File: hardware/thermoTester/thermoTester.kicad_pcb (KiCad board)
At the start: 2 copper layers, 100 x 100 mm, 157 parts, among them J10 Power, J20 PRG, J21 relay, J22 relay, J40 temperature, J41 grating, J42 load, J43 PM9808_TR, J44 key_in, J45 key_in, J46 lamp, J47 lamp, J48 CPTTL, J50 bough, Q30 BC817, Q31 BC817, Q32 BC817, Q50 BC817, Q51 BC817, Q52 BC817, Q53 BC807, Q54 BC817, Q55 BC817, Q56 AO3400, Q60 BC817, Q61 BC817, Q62 BC817, Q63 BC817, Q64 BC817, Q65 BC817, Q66 BC817, U10 XL1509, U11 LM1117-3.3, U20 M_STM32F103RCT6, U21 ULN2003, U22 ULN2003, U40 SP3232, U41 SP3485CN, U50 EL3H4B, Y20 12M

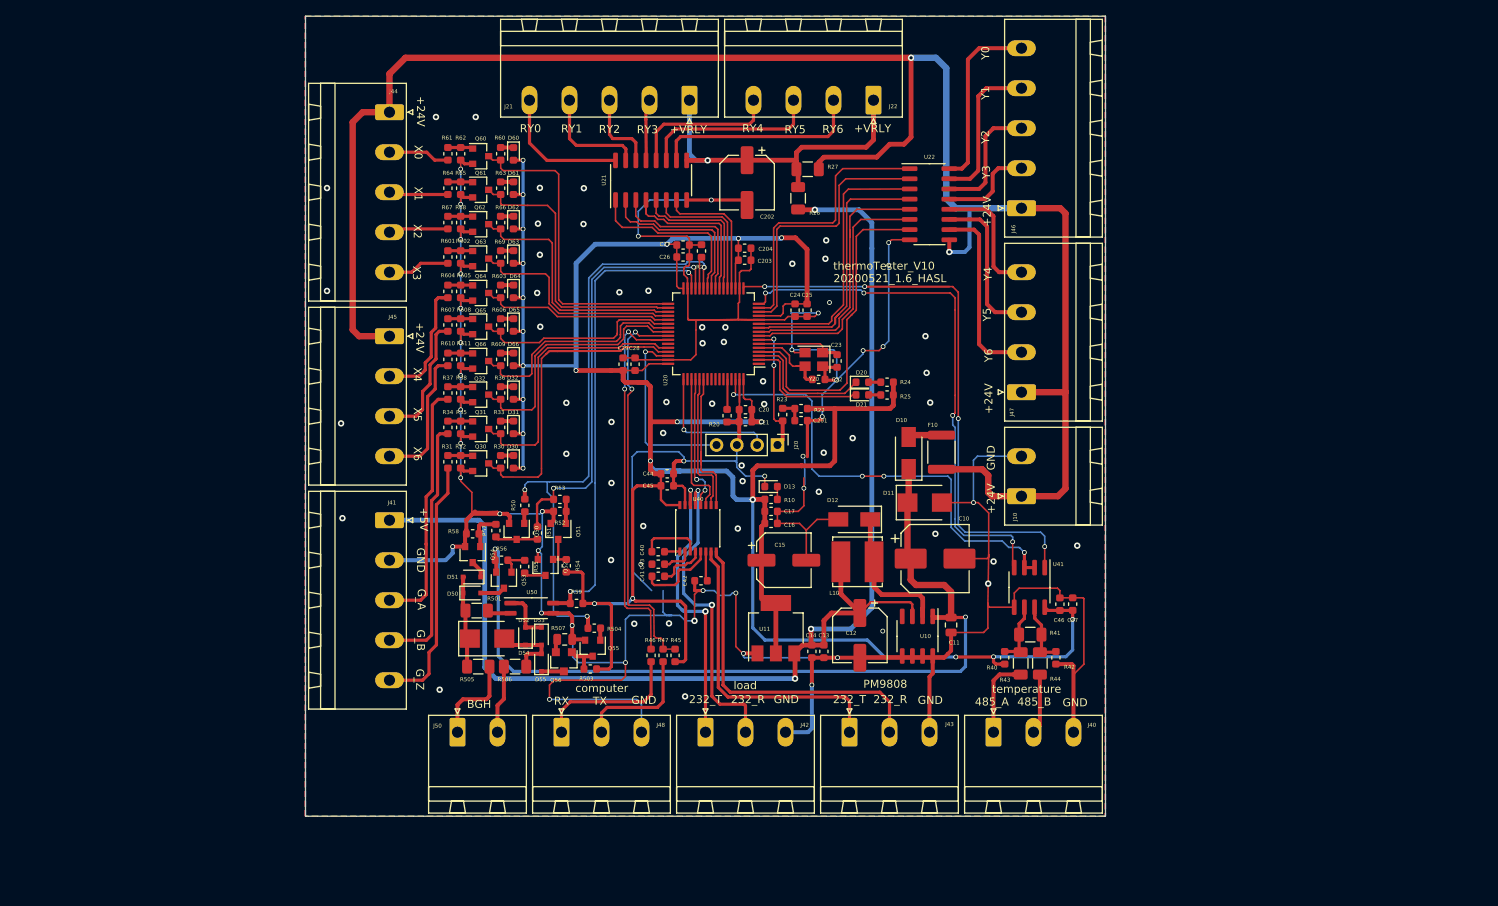
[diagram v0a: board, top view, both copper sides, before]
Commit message: 修改pcb文件，增加外壳支持
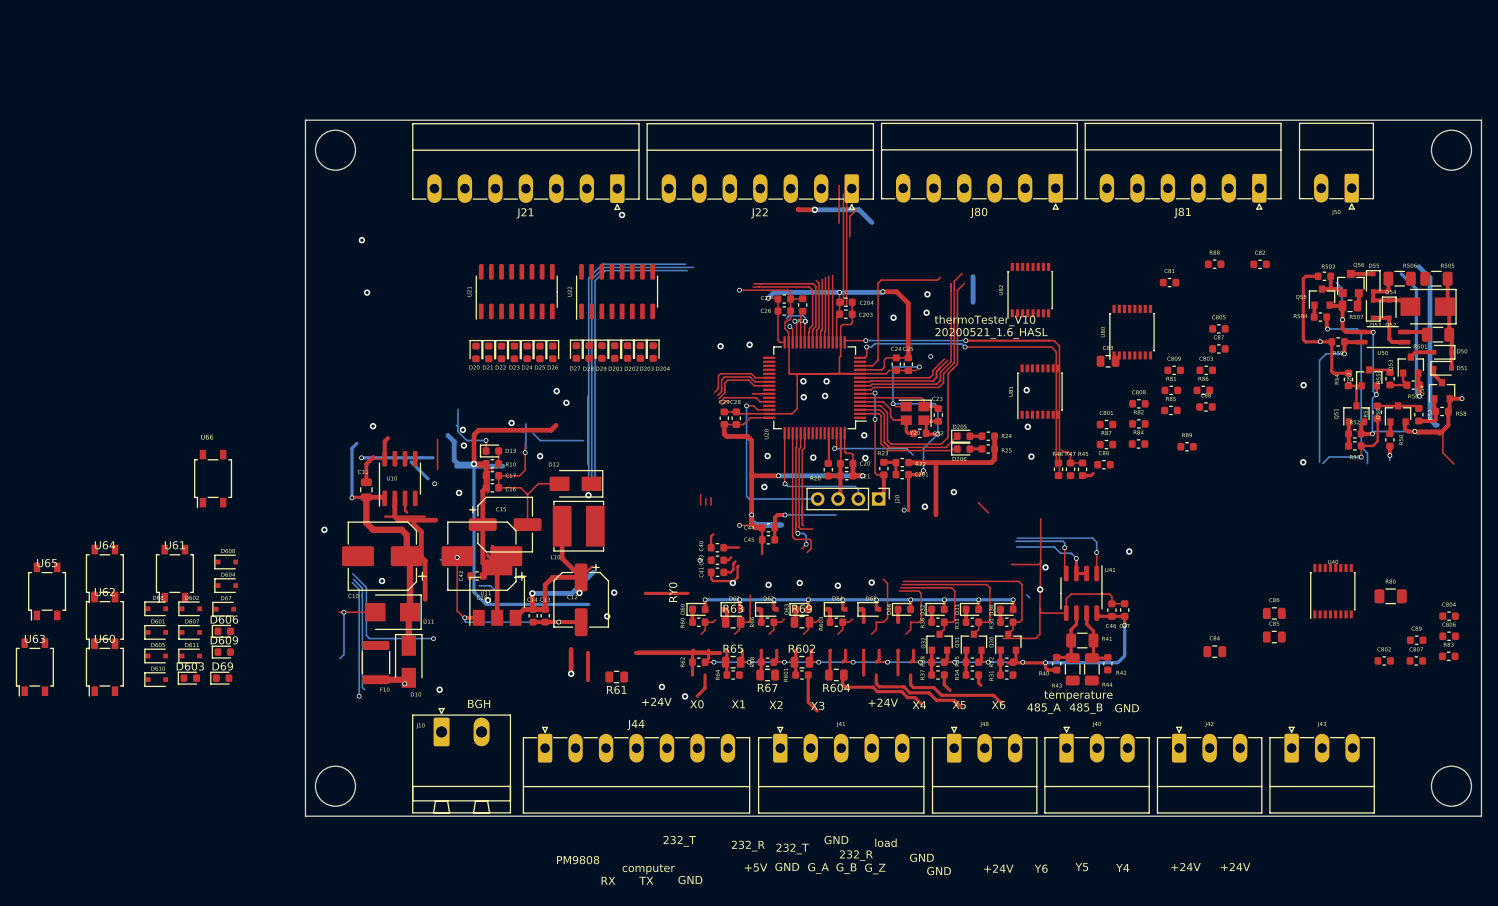
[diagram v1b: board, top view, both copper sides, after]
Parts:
- removed C202: 220uF, kicad_footprint_general:CP_Elec_6.3x5.4
- removed J45: key_in, kicad_footprint_general:PhoenixContact_MSTBA_2,5_4-G_1x04_P5.00mm_Horizontal
- removed J46: lamp, kicad_footprint_general:PhoenixContact_MSTBA_2,5_5-G_1x05_P5.00mm_Horizontal
- removed J47: lamp, kicad_footprint_general:PhoenixContact_MSTBA_2,5_4-G_1x04_P5.00mm_Horizontal
- removed Q60, Q61, Q62, Q63, Q64, Q65, Q66: BC817, kicad_footprint_general:SOT-23
- removed R26: 0, kicad_footprint_general:R_1206_3216Metric
- removed R27: NP(0), kicad_footprint_general:R_1206_3216Metric
- removed R605, R606, R607, R608, R609, R610, R611: 10k, kicad_footprint_general:R_0603_1608Metric
- added C18: 47uF, kicad_footprint_general:CP_Elec_8x6.5, F.Cu at (72.0, 117.5)
- added C80: 47nF, kicad_footprint_general:C_0603_1608Metric, F.Cu at (149.8, 106.1)
- added C801: 47nF, kicad_footprint_general:C_0603_1608Metric, F.Cu at (150.1, 101.0)
- added C802: 47nF, kicad_footprint_general:C_0603_1608Metric, F.Cu at (184.8, 130.6)
- added C803: 47nF, kicad_footprint_general:C_0603_1608Metric, F.Cu at (162.6, 94.3)
- added C804: 47nF, kicad_footprint_general:C_0603_1608Metric, F.Cu at (192.9, 125.0)
- added C805: 47nF, kicad_footprint_general:C_0603_1608Metric, F.Cu at (164.2, 89.1)
- added C806: 100nF, kicad_footprint_general:C_0603_1608Metric, F.Cu at (192.9, 127.5)
- added C807: 1uF, kicad_footprint_general:C_0603_1608Metric, F.Cu at (188.9, 130.6)
- added C808: 1uF, kicad_footprint_general:C_0603_1608Metric, F.Cu at (154.2, 98.5)
- added C809: 100nF, kicad_footprint_general:C_0603_1608Metric, F.Cu at (158.6, 94.3)
- added C81: 47nF, kicad_footprint_general:C_0603_1608Metric, F.Cu at (158.0, 83.3)
- added C82: 47nF, kicad_footprint_general:C_0603_1608Metric, F.Cu at (169.3, 81.0)
- added C83: 100nF, kicad_footprint_general:C_0805_2012Metric, F.Cu at (150.3, 93.1)
- added C84: 100nF, kicad_footprint_general:C_0805_2012Metric, F.Cu at (163.7, 129.4)
- added C85: 100nF, kicad_footprint_general:C_0805_2012Metric, F.Cu at (171.1, 127.6)
- added C86: 100nF, kicad_footprint_general:C_0805_2012Metric, F.Cu at (171.1, 124.7)
- added C87: 47nF, kicad_footprint_general:C_0603_1608Metric, F.Cu at (164.2, 91.6)
- added C88: 47nF, kicad_footprint_general:C_0603_1608Metric, F.Cu at (162.6, 98.8)
- added C89: 47nF, kicad_footprint_general:C_0603_1608Metric, F.Cu at (188.9, 128.0)
- added D201: Red, Diode_SMD:D_0603_1608Metric, F.Cu at (88.7, 92.0)
- added D202: Red, Diode_SMD:D_0603_1608Metric, F.Cu at (90.3, 92.0)
- added D203: Red, Diode_SMD:D_0603_1608Metric, F.Cu at (91.9, 92.0)
- added D204: Red, Diode_SMD:D_0603_1608Metric, F.Cu at (93.5, 92.0)
- added D205: Red, kicad_footprint_general:LED_0603_1608Metric, F.Cu at (132.3, 102.5)
- added D206: Red, kicad_footprint_general:LED_0603_1608Metric, F.Cu at (132.3, 104.1)
- added D22: Red, Diode_SMD:D_0603_1608Metric, F.Cu at (74.5, 92.0)
- added D23: Red, Diode_SMD:D_0603_1608Metric, F.Cu at (76.1, 92.0)
- added D24: Red, Diode_SMD:D_0603_1608Metric, F.Cu at (77.7, 92.0)
- added D25: Red, Diode_SMD:D_0603_1608Metric, F.Cu at (79.3, 92.0)
- added D26: Red, Diode_SMD:D_0603_1608Metric, F.Cu at (80.9, 92.0)
- added D27: Red, Diode_SMD:D_0603_1608Metric, F.Cu at (83.9, 92.0)
- added D28: Red, Diode_SMD:D_0603_1608Metric, F.Cu at (85.5, 92.0)
- added D29: Red, Diode_SMD:D_0603_1608Metric, F.Cu at (87.1, 92.0)
- added D601: 1N4148, kicad_footprint_general:D_SOD-323F, F.Cu at (31.4, 127.0)
- added D602: 1N4148, kicad_footprint_general:D_SOD-323F, F.Cu at (35.7, 124.1)
- added D603: Red, Diode_SMD:D_0603_1608Metric, F.Cu at (35.6, 132.7)
- added D604: 1N4148, kicad_footprint_general:D_SOD-323F, F.Cu at (40.2, 121.2)
- added D605: 1N4148, kicad_footprint_general:D_SOD-323F, F.Cu at (31.4, 130.0)
- added D606: Red, Diode_SMD:D_0603_1608Metric, F.Cu at (39.8, 126.9)
- added D607: 1N4148, kicad_footprint_general:D_SOD-323F, F.Cu at (35.7, 127.0)
- added D608: 1N4148, kicad_footprint_general:D_SOD-323F, F.Cu at (40.2, 118.2)
- added D609: Red, Diode_SMD:D_0603_1608Metric, F.Cu at (39.8, 129.5)
- added D610: 1N4148, kicad_footprint_general:D_SOD-323F, F.Cu at (31.4, 132.9)
- added D611: 1N4148, kicad_footprint_general:D_SOD-323F, F.Cu at (35.7, 130.0)
- added D67: 1N4148, kicad_footprint_general:D_SOD-323F, F.Cu at (39.9, 124.1)
- added D68: 1N4148, kicad_footprint_general:D_SOD-323F, F.Cu at (31.4, 124.1)
- added D69: Red, Diode_SMD:D_0603_1608Metric, F.Cu at (39.6, 132.7)
- added J80: PT100, kicad_footprint_general:PhoenixContact_MC_1,5_6-G-3.81_1x06_P3.81mm_Horizontal, F.Cu at (143.8, 71.5)
- added J81: PT100, kicad_footprint_general:PhoenixContact_MC_1,5_6-G-3.81_1x06_P3.81mm_Horizontal, F.Cu at (169.2, 71.5)
- added R80: 100R, kicad_footprint_general:R_1206_3216Metric, F.Cu at (185.6, 122.5)
- added R81: 4.7k, kicad_footprint_general:R_0603_1608Metric, F.Cu at (158.2, 96.8)
- added R82: 4.7k, kicad_footprint_general:R_0603_1608Metric, F.Cu at (154.2, 101.0)
- added R83: 4.7k, kicad_footprint_general:R_0603_1608Metric, F.Cu at (192.9, 130.0)
- added R84: 4.7k, kicad_footprint_general:R_0603_1608Metric, F.Cu at (154.1, 103.5)
- added R85: 4.7k, kicad_footprint_general:R_0603_1608Metric, F.Cu at (158.2, 99.3)
- added R86: 4.7k, kicad_footprint_general:R_0603_1608Metric, F.Cu at (162.2, 96.8)
- added R87: 4.7k, kicad_footprint_general:R_0603_1608Metric, F.Cu at (150.1, 103.6)
- added R88: 4.7k, kicad_footprint_general:R_0603_1608Metric, F.Cu at (163.7, 81.0)
- added R89: 4.7k, kicad_footprint_general:R_0603_1608Metric, F.Cu at (160.2, 103.8)
- added U60: EL357N, kicad_footprint_general:SO-4_4.4x4.3mm_P2.54mm, F.Cu at (24.9, 131.4)
- added U61: EL357N, kicad_footprint_general:SO-4_4.4x4.3mm_P2.54mm, F.Cu at (33.7, 119.7)
- added U62: EL357N, kicad_footprint_general:SO-4_4.4x4.3mm_P2.54mm, F.Cu at (24.9, 125.5)
- added U63: EL357N, kicad_footprint_general:SO-4_4.4x4.3mm_P2.54mm, F.Cu at (16.2, 131.4)
- added U64: EL357N, kicad_footprint_general:SO-4_4.4x4.3mm_P2.54mm, F.Cu at (24.9, 119.7)
- added U65: EL357N, kicad_footprint_general:SO-4_4.4x4.3mm_P2.54mm, F.Cu at (17.7, 121.9)
- added U66: EL357N, kicad_footprint_general:SO-4_4.4x4.3mm_P2.54mm, F.Cu at (38.5, 107.8)
- added U80: ADS1220IPWR, kicad_footprint_general:SSOP-16_4.4x5.2mm_P0.65mm, F.Cu at (153.3, 89.5)
- added U81: CD4051B, kicad_footprint_general:SSOP-16_4.4x5.2mm_P0.65mm, F.Cu at (141.8, 96.9)
- added U82: CD4052B, kicad_footprint_general:SSOP-16_4.4x5.2mm_P0.65mm, F.Cu at (140.6, 84.2)
- D20, D21: footprint kicad_footprint_general:LED_0603_1608Metric -> Diode_SMD:D_0603_1608Metric
- D61, D62, D64, D65: value Red -> 1N4148; footprint Diode_SMD:D_0603_1608Metric -> kicad_footprint_general:D_SOD-323F
- J21: value relay -> YOUT; footprint kicad_footprint_general:PhoenixContact_MSTBA_2,5_5-G_1x05_P5.00mm_Horizontal -> kicad_footprint_general:PhoenixContact_MC_1,5_7-G-3.81_1x07_P3.81mm_Horizontal
- J22: value relay -> YOUT; footprint kicad_footprint_general:PhoenixContact_MSTBA_2,5_4-G_1x04_P5.00mm_Horizontal -> kicad_footprint_general:PhoenixContact_MC_1,5_7-G-3.81_1x07_P3.81mm_Horizontal
- J40, J42: footprint kicad_footprint_general:PhoenixContact_MSTBA_2,5_3-G_1x03_P5.00mm_Horizontal -> kicad_footprint_general:PhoenixContact_MC_1,5_3-G-3.81_1x03_P3.81mm_Horizontal
- J41: footprint kicad_footprint_general:PhoenixContact_MSTBA_2,5_5-G_1x05_P5.00mm_Horizontal -> kicad_footprint_general:PhoenixContact_MC_1,5_5-G-3.81_1x05_P3.81mm_Horizontal
- J43, J48: footprint Connector_Phoenix_MSTB:PhoenixContact_MSTBA_2,5_3-G_1x03_P5.00mm_Horizontal -> kicad_footprint_general:PhoenixContact_MC_1,5_3-G-3.81_1x03_P3.81mm_Horizontal
- J44: value key_in -> XIN; footprint kicad_footprint_general:PhoenixContact_MSTBA_2,5_5-G_1x05_P5.00mm_Horizontal -> kicad_footprint_general:PhoenixContact_MC_1,5_7-G-3.81_1x07_P3.81mm_Horizontal
- J50: footprint kicad_footprint_general:PhoenixContact_MSTBA_2,5_2-G_1x02_P5.00mm_Horizontal -> kicad_footprint_general:PhoenixContact_MC_1,5_2-G-3.81_1x02_P3.81mm_Horizontal
- R60, R601, R603, R62, R64, R66, R68: value 10k -> 2.7k
- R602, R604, R61, R63, R65, R67, R69: value 10k -> 7.5k; footprint kicad_footprint_general:R_0603_1608Metric -> kicad_footprint_general:R_0805_2012Metric
- moved J50 130.8 mm to (180.8, 71.5), turned to 180 degrees
- moved R505 129.2 mm to (191.4, 82.8), turned to 0 degrees
- moved D50 125.0 mm to (192.2, 92.0), turned to 180 degrees
- moved R501 125.0 mm to (191.6, 89.8), turned to 0 degrees
- moved D54 124.7 mm to (190.3, 86.3), turned to 180 degrees
- moved D51 124.1 mm to (192.2, 94.0), turned to 0 degrees
- moved Q54 122.9 mm to (192.1, 96.8), turned to 270 degrees
- moved R58 122.1 mm to (192.1, 99.4), turned to 0 degrees
- moved R506 120.7 mm to (186.8, 82.8), turned to 180 degrees
- moved Q53 116.5 mm to (188.2, 93.6), turned to 270 degrees
- moved R57 116.3 mm to (189.2, 99.8), turned to 270 degrees
- moved R56 116.1 mm to (188.5, 96.1), turned to 180 degrees
- moved D52 115.5 mm to (185.5, 86.6), turned to 270 degrees
- moved D55 114.3 mm to (183.5, 83.3), turned to 270 degrees
- moved D53 111.7 mm to (183.5, 86.6), turned to 90 degrees
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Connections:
- net /MVGS renamed /M_X0
- D20 pad 1: /LED0 -> Net-(D20-Pad1)
- D20 pad 2: Net-(D20-Pad2) -> /M_Y0
- D21 pad 1: /LED1 -> Net-(D21-Pad1)
- D21 pad 2: Net-(D21-Pad2) -> /M_Y1
- D61 pad 2: VCC -> Net-(D61-Pad2)
- D62 pad 1: Net-(D62-Pad1) -> /X0
- D62 pad 2: VCC -> Net-(D61-Pad2)
- D64 pad 2: VCC -> Net-(D64-Pad2)
- D65 pad 1: Net-(D65-Pad1) -> /X1
- D65 pad 2: VCC -> Net-(D64-Pad2)
- J21 pad 1: /VRLY -> /Y6
- J21 pad 2: /C_CK3 -> /Y5
- J21 pad 3: /C_CK2 -> /Y4
- J21 pad 4: /C_CK1 -> /Y3
- J21 pad 5: /C_CK0 -> /Y2
- J22 pad 1: /VRLY -> /Y13
- J22 pad 2: /C_CK6 -> /Y12
- J22 pad 3: /C_CK5 -> /Y11
- J22 pad 4: /C_CK4 -> /Y10
- J44 pad 1: /VIN -> /X0
- J44 pad 2: /voltage_s -> /X1
- J44 pad 3: /start -> /X2
- J44 pad 4: /stop -> /X3
- J44 pad 5: /key_rsv1 -> /X4
- R24 pad 2: Net-(D20-Pad2) -> Net-(D205-Pad2)
- R25 pad 2: Net-(D21-Pad2) -> Net-(D206-Pad2)
- R507 pad 1: GND -> /OVLD
- R507 pad 2: /OVLD -> GND
- R601 pad 1: /key_rsv1 -> Net-(D606-Pad1)
- R601 pad 2: Net-(Q63-Pad1) -> /M_X5
- R602 pad 1: Net-(Q63-Pad1) -> Net-(D607-Pad1)
- R602 pad 2: GND -> VDD
- R603 pad 1: Net-(D64-Pad1) -> Net-(D609-Pad1)
- R603 pad 2: /MKSV2 -> /M_X6
- R604 pad 1: /key_rsv2 -> Net-(D610-Pad1)
- R604 pad 2: Net-(Q64-Pad1) -> VDD
- R61 pad 1: /voltage_s -> Net-(D61-Pad1)
- R61 pad 2: Net-(Q60-Pad1) -> VDD
- R62 pad 1: Net-(Q60-Pad1) -> Net-(D63-Pad1)
- R62 pad 2: GND -> /M_X1
- R63 pad 1: Net-(D61-Pad1) -> Net-(D64-Pad1)
- R63 pad 2: /MSTR -> VDD
- R64 pad 1: /start -> Net-(D66-Pad1)
- R64 pad 2: Net-(Q61-Pad1) -> /M_X2
- R65 pad 1: Net-(Q61-Pad1) -> Net-(D67-Pad1)
- R65 pad 2: GND -> VDD
- R66 pad 1: Net-(D62-Pad1) -> Net-(D69-Pad1)
- R66 pad 2: /MSTP -> /M_X3
- R67 pad 1: /stop -> Net-(D601-Pad1)
- R67 pad 2: Net-(Q62-Pad1) -> VDD
- R68 pad 1: Net-(Q62-Pad1) -> Net-(D603-Pad1)
- R68 pad 2: GND -> /M_X4
- R69 pad 1: Net-(D63-Pad1) -> Net-(D604-Pad1)
- R69 pad 2: /MKSV1 -> VDD
- U20 pad 10: /MLs2 -> /M_Y10
- U20 pad 11: /MLs1 -> /M_Y9
- U20 pad 14: /Mtest -> /M_Y8
- U20 pad 15: /Mrun -> /M_Y7
- U20 pad 20: /M_CK6 -> /M_Y6
- U20 pad 21: /M_CK5 -> /M_Y5
- U20 pad 22: /M_CK4 -> /M_Y4
- U20 pad 23: /M_CK3 -> /M_Y3
- U20 pad 24: /M_CK2 -> /M_Y2
- U20 pad 25: /M_CK1 -> /M_Y1
- U20 pad 26: /M_CK0 -> /M_Y0
- U20 pad 34: /MSTR -> /M_X1
- U20 pad 35: /MSTP -> /M_X2
- U20 pad 36: /MKSV1 -> /M_X3
- U20 pad 37: /MKSV2 -> /M_X4
- U20 pad 38: /MKSV3 -> /M_X5
- U20 pad 39: /MKSV4 -> /M_X6
- U20 pad 4: /MLs5 -> /M_Y13
- U20 pad 41: /MTX1 -> Net-(U20-Pad41)
- U20 pad 42: /MRX1 -> /MTX1
- U20 pad 43: Net-(U20-Pad43) -> /MRX1
- U20 pad 50: Net-(U20-Pad50) -> /DOUT
- U20 pad 55: Net-(U20-Pad55) -> /SCLK
- U20 pad 56: Net-(U20-Pad56) -> /DIN
- U20 pad 57: Net-(U20-Pad57) -> /RDY
- U20 pad 58: Net-(U20-Pad58) -> /SL1
- U20 pad 59: Net-(U20-Pad59) -> /SL0
- U20 pad 61: Net-(U20-Pad61) -> /SL2
- U20 pad 8: /MLs4 -> /M_Y12
- U20 pad 9: /MLs3 -> /M_Y11
- U21 pad 1: /M_CK0 -> Net-(D20-Pad1)
- U21 pad 10: /C_CK6 -> /Y6
- U21 pad 11: /C_CK5 -> /Y5
- U21 pad 12: /C_CK4 -> /Y4
- U21 pad 13: /C_CK3 -> /Y3
- U21 pad 14: /C_CK2 -> /Y2
- U21 pad 15: /C_CK1 -> /Y1
- U21 pad 16: /C_CK0 -> /Y0
- U21 pad 2: /M_CK1 -> Net-(D21-Pad1)
- U21 pad 3: /M_CK2 -> Net-(D22-Pad1)
- U21 pad 4: /M_CK3 -> Net-(D23-Pad1)
- U21 pad 5: /M_CK4 -> Net-(D24-Pad1)
- U21 pad 6: /M_CK5 -> Net-(D25-Pad1)
- U21 pad 7: /M_CK6 -> Net-(D26-Pad1)
- U21 pad 9: /VRLY -> /VIN
- U22 pad 1: /Mrun -> Net-(D27-Pad1)
- U22 pad 10: /lamp_rsv5 -> /Y13
- U22 pad 11: /lamp_rsv4 -> /Y12
- U22 pad 12: /lamp_rsv3 -> /Y11
- U22 pad 13: /lamp_rsv2 -> /Y10
- U22 pad 14: /lamp_rsv1 -> /Y9
- U22 pad 15: /test -> /Y8
- U22 pad 16: /run -> /Y7
- U22 pad 2: /Mtest -> Net-(D28-Pad1)
- U22 pad 3: /MLs1 -> Net-(D29-Pad1)
- U22 pad 4: /MLs2 -> Net-(D201-Pad1)
- U22 pad 5: /MLs3 -> Net-(D202-Pad1)
- U22 pad 6: /MLs4 -> Net-(D203-Pad1)
- U22 pad 7: /MLs5 -> Net-(D204-Pad1)
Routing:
- net /VIN: track 235.0 -> 0.00 mm, vias 2 -> 0
- net GND: track 615.8 -> 406.2 mm, vias 92 -> 80
- net +5VD: track 169.5 -> 71.2 mm
- net VCC: track 465.3 -> 387.5 mm, vias 23 -> 22
- net /MRX1: track 50.2 -> 0.00 mm, vias 2 -> 0
- net /MTX1: track 49.9 -> 6.06 mm, vias 2 -> 0
- net /VRLY: track 43.7 -> 0.00 mm, vias 1 -> 0
- net /MLs5: track 43.4 -> 0.00 mm
- net /RS3_R: track 42.5 -> 0.00 mm
- net /RS2_R: track 39.1 -> 0.00 mm, vias 2 -> 1
- net /RS3_T: track 38.4 -> 0.00 mm
- net /M_Y13: track 0.00 -> 37.6 mm
- net /M_X0: track 39.9 -> 3.14 mm
- net /RS2_T: track 35.9 -> 0.00 mm, vias 2 -> 0
- net /MSTR: track 35.6 -> 0.00 mm
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- removed copper zone on B.Cu, net GND
- removed copper zone on F.Cu, net GND
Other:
- board size 100 x 100 mm -> 147 x 87 mm
- board text removed: "+VRLY"
- board text removed: "RY1"
- board text removed: "RY2"
- board text removed: "RY3"
- board text removed: "RY4"
- board text removed: "RY5"
- board text removed: "RY6"
- board text removed: "Y0"
- board text removed: "Y1"
- board text removed: "Y2"
- board text removed: "Y3"

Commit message: Pcb manufactured in jlc
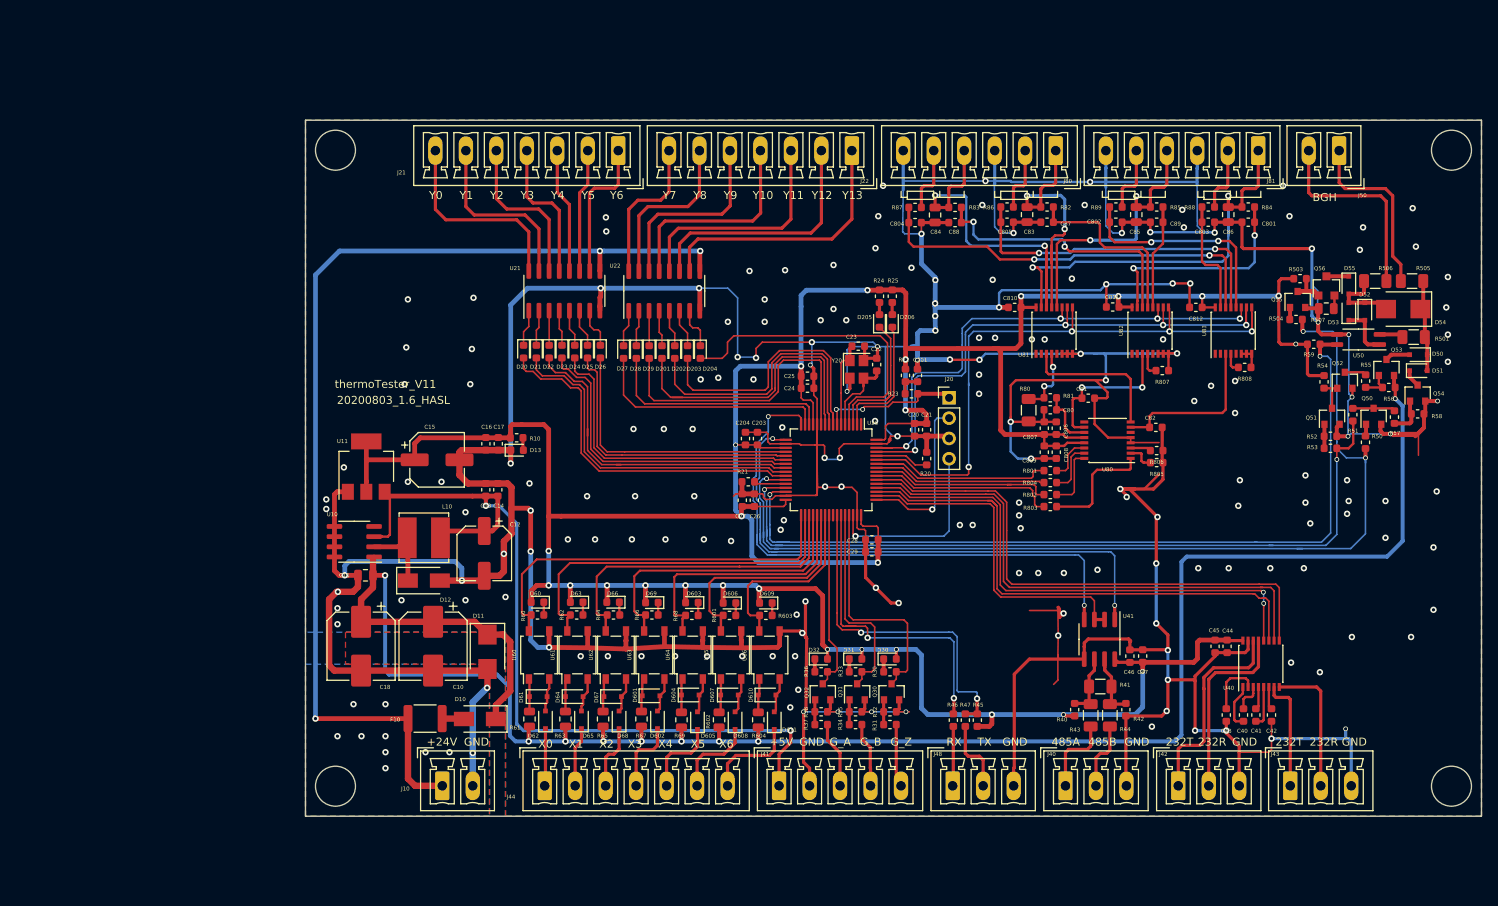
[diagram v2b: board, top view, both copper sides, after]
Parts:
- added C810: 100nF, kicad_footprint_general:C_0603_1608Metric, F.Cu at (138.7, 86.4)
- added C811: 100nF, kicad_footprint_general:C_0603_1608Metric, F.Cu at (150.9, 86.3)
- added C812: 100nF, kicad_footprint_general:C_0603_1608Metric, F.Cu at (161.3, 86.4)
- added R801: 47R, kicad_footprint_general:R_0603_1608Metric, F.Cu at (143.1, 106.8)
- added R802: 47R, kicad_footprint_general:R_0603_1608Metric, F.Cu at (143.1, 109.8)
- added R803: 47R, kicad_footprint_general:R_0603_1608Metric, F.Cu at (143.1, 111.3)
- added R804: 47R, kicad_footprint_general:R_0603_1608Metric, F.Cu at (143.1, 108.3)
- added R805: 47R, kicad_footprint_general:R_0603_1608Metric, F.Cu at (156.4, 105.8)
- added R806: 47R, kicad_footprint_general:R_0603_1608Metric, F.Cu at (156.4, 104.3)
- added R807: 47R, kicad_footprint_general:R_0603_1608Metric, F.Cu at (157.1, 94.3)
- added R808: 47R, kicad_footprint_general:R_0603_1608Metric, F.Cu at (167.4, 93.9)
- added U83: CD4051B, kicad_footprint_general:SSOP-16_4.4x5.2mm_P0.65mm, F.Cu at (166.0, 89.3)
- F10: value 100mA -> 200mA
- J10: footprint kicad_footprint_general:PhoenixContact_MSTBA_2,5_2-G_1x02_P5.00mm_Horizontal -> kicad_footprint_general:PhoenixContact_MCV_1,5_2-G-3.81_1x02_P3.81mm_Vertical
- J21, J22, J44: footprint kicad_footprint_general:PhoenixContact_MC_1,5_7-G-3.81_1x07_P3.81mm_Horizontal -> kicad_footprint_general:PhoenixContact_MCV_1,5_7-G-3.81_1x07_P3.81mm_Vertical
- J40, J42, J43, J48: footprint kicad_footprint_general:PhoenixContact_MC_1,5_3-G-3.81_1x03_P3.81mm_Horizontal -> kicad_footprint_general:PhoenixContact_MCV_1,5_3-G-3.81_1x03_P3.81mm_Vertical
- J41: footprint kicad_footprint_general:PhoenixContact_MC_1,5_5-G-3.81_1x05_P3.81mm_Horizontal -> kicad_footprint_general:PhoenixContact_MCV_1,5_5-G-3.81_1x05_P3.81mm_Vertical
- J50: footprint kicad_footprint_general:PhoenixContact_MC_1,5_2-G-3.81_1x02_P3.81mm_Horizontal -> kicad_footprint_general:PhoenixContact_MCV_1,5_2-G-3.81_1x02_P3.81mm_Vertical
- J80, J81: footprint kicad_footprint_general:PhoenixContact_MC_1,5_6-G-3.81_1x06_P3.81mm_Horizontal -> kicad_footprint_general:PhoenixContact_MCV_1,5_6-G-3.81_1x06_P3.81mm_Vertical
- Q56: value AO3400 -> AO3422
- U82: value CD4052B -> CD4051B
- moved C42 100.8 mm to (170.8, 137.3), turned to 270 degrees
- moved U65 85.9 mm to (103.2, 129.8), turned to 90 degrees
- moved R83 83.4 mm to (131.2, 73.9), turned to 180 degrees
- moved C804 82.9 mm to (126.2, 75.8)
- moved U63 77.4 mm to (93.6, 129.8), turned to 90 degrees
- moved D610 76.3 mm to (107.7, 134.8)
- moved U64 74.2 mm to (98.4, 129.8), turned to 90 degrees
- moved D611 73.4 mm to (108.6, 138.1), turned to 90 degrees
- moved U66 73.0 mm to (108.0, 129.8), turned to 90 degrees
- moved C41 69.6 mm to (168.8, 137.3), turned to 270 degrees
- moved C40 69.0 mm to (167.2, 137.3), turned to 90 degrees
- moved D605 68.1 mm to (99.0, 138.1), turned to 90 degrees
- moved D609 68.0 mm to (107.5, 123.3), turned to 180 degrees
- moved D607 67.8 mm to (103.0, 134.8)
- moved D608 66.5 mm to (103.7, 138.1), turned to 90 degrees
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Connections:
- U20 pad 50: /DOUT -> /TR_S1
- U20 pad 57: /RDY -> /DOUT
- U20 pad 58: /SL1 -> /RDY
- U20 pad 59: /SL0 -> /SL2
- U20 pad 61: /SL2 -> /SL1
- U20 pad 62: /TR_S1 -> /SL0
- U80 pad 1: /SCLK -> Net-(R803-Pad2)
- U80 pad 14: /RDY -> Net-(R801-Pad2)
- U80 pad 15: /DOUT -> Net-(R804-Pad2)
- U80 pad 16: /DIN -> Net-(R802-Pad2)
- U80 pad 2: GND -> Net-(R805-Pad2)
- U80 pad 3: GND -> Net-(R806-Pad2)
- U82 pad 1: Net-(C805-Pad1) -> Net-(U82-Pad1)
- U82 pad 10: /SL0 -> /SL1
- U82 pad 11: Net-(C89-Pad1) -> /SL0
- U82 pad 12: Net-(C87-Pad2) -> Net-(C89-Pad1)
- U82 pad 13: /AIN1 -> Net-(C87-Pad2)
- U82 pad 2: Net-(C803-Pad1) -> Net-(U82-Pad2)
- U82 pad 3: /AIN2 -> /AIN1
- U82 pad 4: Net-(C802-Pad1) -> Net-(R807-Pad2)
- U82 pad 5: Net-(C804-Pad1) -> Net-(U82-Pad5)
- U82 pad 9: /SL1 -> /SL2
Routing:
- net GND: track 406.2 -> 1018.1 mm, vias 80 -> 205
- net VDD: track 79.1 -> 243.7 mm, vias 2 -> 9
- net /VIN: track 0.00 -> 133.6 mm, vias 0 -> 3
- net VCC: track 387.5 -> 476.4 mm, vias 22 -> 26
- net /SL2: track 0.00 -> 77.0 mm, vias 0 -> 4
- net /SL1: track 0.00 -> 69.6 mm, vias 0 -> 4
- net /SL0: track 0.00 -> 65.9 mm, vias 0 -> 4
- net /TRS: track 68.2 -> 124.8 mm
- net /P2_L1: track 0.00 -> 55.2 mm, vias 0 -> 2
- net Net-(C804-Pad1): track 0.00 -> 51.3 mm, vias 0 -> 2
- net /MTX5: track 17.6 -> 67.4 mm
- net /MTX4: track 18.0 -> 67.3 mm
- net /MRX5: track 19.0 -> 68.2 mm
- net /MRX3: track 59.6 -> 108.2 mm
- net /MRX4: track 17.5 -> 65.7 mm
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- added copper zone on B.Cu, net GND
- added copper zone on F.Cu, net GND
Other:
- board text added: "20200803_1.6_HASL"
- board text added: "232R"
- board text added: "232T"
- board text added: "485A"
- board text added: "485B"
- board text added: "Y0"
- board text added: "Y1"
- board text added: "Y10"
- board text added: "Y11"
- board text added: "Y12"
- board text added: "Y13"
- board text added: "Y2"
- board text added: "Y3"
- board text added: "Y7"
- board text added: "Y8"
- board text added: "Y9"
- board text added: "thermoTester_V11"
- board text removed: "20200521_1.6_HASL"
- board text removed: "232_R"
- board text removed: "232_T"
- board text removed: "485_A"
- board text removed: "485_B"
- board text removed: "PM9808"
- board text removed: "RY0"
- board text removed: "computer"
- board text removed: "load"
- board text removed: "temperature"
- board text removed: "thermoTester_V10"
